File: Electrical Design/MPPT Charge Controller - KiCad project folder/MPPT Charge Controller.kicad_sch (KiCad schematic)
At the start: 70 parts, among them J1 Conn_01x02_Socket, J2 Conn_01x02_Socket, J3 Conn_01x02_Socket, Q1 Q_Dual_NMOS_S1G1S2G2D2D2D1D1, Q2 Q_Dual_NMOS_S1G1S2G2D2D2D1D1, Q3 2N7002, U2 AP63203WU, U3 ACS712, U4 ACS712, U5 MCP4018

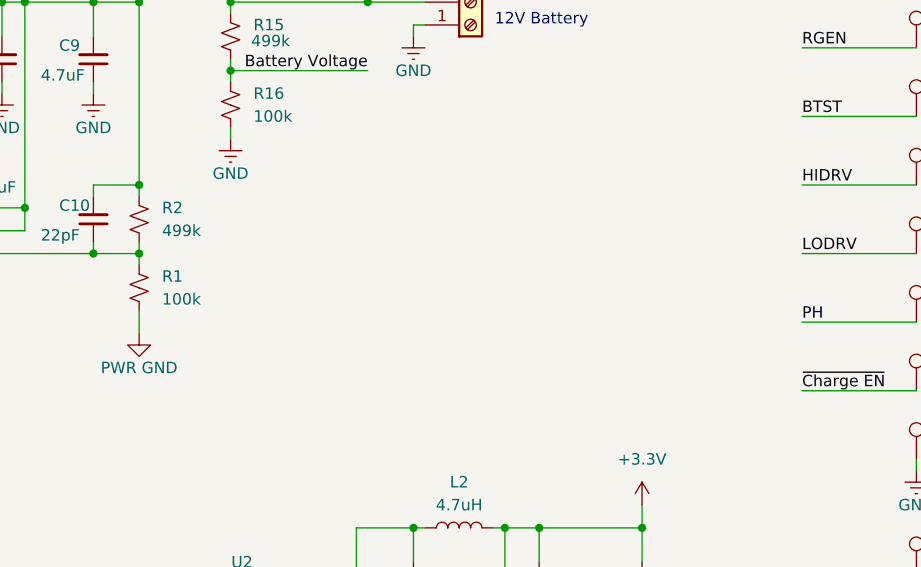
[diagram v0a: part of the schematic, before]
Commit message: update VBAT to 3.5V for single LiFePO4 cell
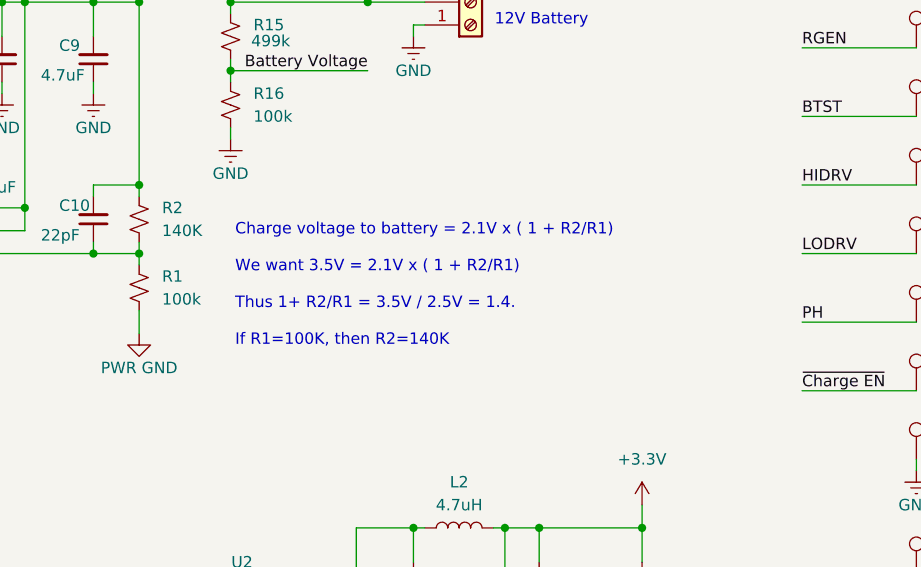
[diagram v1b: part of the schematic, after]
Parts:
- R2: value 499k -> 140K
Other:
- note added: "Charge voltage to battery = 2.1V x ( 1 + R2/R1) We want 3.5V = 2.1V x ( 1 + R2/R1) Thus 1+ R2/R1 = 3.5V / 2.5V = 1.4. If R1=100K, then R2=140K"
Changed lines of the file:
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@@
 	(title_block
 		(title "MPPT Charge Controller")
-		(rev "0.3")
+		(rev "20250209")
+		(comment 1 "Adapted for MEGAphone module format")
+		(comment 2 "Adapted for 3.5V output voltage")
 	)
 	(junction
@@
 		)
 	)
+	(text "Charge voltage to battery = 2.1V x ( 1 + R2/R1)\n\nWe want 3.5V = 2.1V x ( 1 + R2/R1)\n\nThus 1+ R2/R1 = 3.5V / 2.5V = 1.4.\n\nIf R1=100K, then R2=140K"
+		(exclude_from_sim no)
+		(at 194.818 102.616 0)
+		(effects
+			(font
+				(size 1.27 1.27)
+			)
+			(justify left)
+		)
+	)
 	(text "connected to GND\nthrough board vias"
 		(exclude_from_sim no)
@@
 	(label "STAT1"
 		(at 74.93 135.89 0)
-		(fields_autoplaced yes)
 		(effects
 			(font
@@
 	(label "BTST"
 		(at 257.81 83.82 0)
-		(fields_autoplaced yes)
 		(effects
 			(font
@@
 	(label "TS"
 		(at 257.81 43.18 0)
-		(fields_autoplaced yes)
 		(effects
 			(font
@@
 	(label "VCC"
 		(at 257.81 20.32 0)
-		(fields_autoplaced yes)
 		(effects
 			(font
@@
 	(label "SD_CS"
 		(at 74.93 143.51 0)
-		(fields_autoplaced yes)
 		(effects
 			(font
@@
 	(label "~{Charge EN}"
 		(at 74.93 140.97 0)
-		(fields_autoplaced yes)
 		(effects
 			(font
@@
 	(label "Input"
 		(at 34.29 45.72 0)
-		(fields_autoplaced yes)
 		(effects
 			(font
@@
 	(label "SCL"
 		(at 17.78 81.28 0)
-		(fields_autoplaced yes)
 		(effects
 			(font
@@
 	(label "Battery Voltage"
 		(at 209.55 78.74 180)
-		(fields_autoplaced yes)
 		(effects
 			(font
@@
 	(label "Solar Voltage"
 		(at 55.88 53.34 180)
-		(fields_autoplaced yes)
 		(effects
 			(font
@@
 	(label "Load Enable"
 		(at 240.03 55.88 180)
-		(fields_autoplaced yes)
 		(effects
 			(font
@@
 	(label "~{Charge EN}"
 		(at 52.07 78.74 0)
-		(fields_autoplaced yes)
 		(effects
 			(font
@@
 	(label "LODRV"
 		(at 257.81 99.06 0)
-		(fields_autoplaced yes)
 		(effects
 			(font
@@
 	(label "STAT2"
 		(at 257.81 67.31 0)
-		(fields_autoplaced yes)
 		(effects
 			(font
@@
 	(label "Load Enable"
 		(at 74.93 146.05 0)
-		(fields_autoplaced yes)
 		(effects
 			(font
@@
 	(label "HIDRV"
 		(at 257.81 91.44 0)
-		(fields_autoplaced yes)
 		(effects
 			(font
@@
 	(label "VCC"
 		(at 116.84 60.96 0)
-		(fields_autoplaced yes)
 		(effects
 			(font
@@
 	(label "Solar Voltage"
 		(at 134.62 151.13 180)
-		(fields_autoplaced yes)
 		(effects
 			(font
@@
 	(label "VREF"
 		(at 80.01 64.77 0)
-		(fields_autoplaced yes)
 		(effects
 			(font
@@
 	(label "MPPSET"
 		(at 71.12 72.39 0)
-		(fields_autoplaced yes)
 		(effects
 			(font
@@
 	(label "STAT2"
 		(at 83.82 99.06 180)
-		(fields_autoplaced yes)
 		(effects
 			(font
@@
 	(label "RGEN"
 		(at 257.81 76.2 0)
-		(fields_autoplaced yes)
 		(effects
 			(font
@@
 	(label "VFB"
 		(at 115.57 96.52 0)
-		(fields_autoplaced yes)
 		(effects
 			(font
@@
 	(label "Solar Current"
 		(at 31.75 19.05 0)
-		(fields_autoplaced yes)
 		(effects
 			(font
@@
 	(label "BTST"
 		(at 139.7 41.91 180)
-		(fields_autoplaced yes)
 		(effects
 			(font
@@
 	(label "VFB"
 		(at 257.81 50.8 0)
-		(fields_autoplaced yes)
 		(effects
 			(font
@@
 	(label "VIN"
 		(at 59.69 45.72 0)
-		(fields_autoplaced yes)
 		(effects
 			(font
@@
 	(label "TS"
 		(at 71.12 113.03 0)
-		(fields_autoplaced yes)
 		(effects
 			(font
@@
 	(label "HIDRV"
 		(at 116.84 53.34 0)
-		(fields_autoplaced yes)
 		(effects
 			(font
@@
 	(label "VIN"
 		(at 177.8 140.97 0)
-		(fields_autoplaced yes)
 		(effects
 			(font
@@
 	(label "Battery Voltage"
 		(at 134.62 156.21 180)
-		(fields_autoplaced yes)
 		(effects
 			(font
@@
 	(label "VREF"
 		(at 57.15 92.71 0)
-		(fields_autoplaced yes)
 		(effects
 			(font
@@
 	(label "Battery Current"
 		(at 134.62 158.75 180)
-		(fields_autoplaced yes)
 		(effects
 			(font
@@
 	(label "Input"
 		(at 257.81 135.89 0)
-		(fields_autoplaced yes)
 		(effects
 			(font
@@
 	(label "LODRV"
 		(at 116.84 81.28 0)
-		(fields_autoplaced yes)
 		(effects
 			(font
@@
 	(label "SDA"
 		(at 17.78 83.82 0)
-		(fields_autoplaced yes)
 		(effects
 			(font
@@
 	(label "STAT1"
 		(at 83.82 92.71 180)
-		(fields_autoplaced yes)
 		(effects
 			(font
@@
 	(label "~{Charge EN}"
 		(at 257.81 114.3 0)
-		(fields_autoplaced yes)
 		(effects
 			(font
@@
 	(label "RGEN"
 		(at 116.84 64.77 0)
-		(fields_autoplaced yes)
 		(effects
 			(font
@@
 	(label "STAT2"
 		(at 74.93 138.43 0)
-		(fields_autoplaced yes)
 		(effects
 			(font
@@
 	(label "PH"
 		(at 115.57 76.2 0)
-		(fields_autoplaced yes)
 		(effects
 			(font
@@
 	(label "VREF"
 		(at 257.81 27.94 0)
-		(fields_autoplaced yes)
 		(effects
 			(font
@@
 	(label "MPPSET"
 		(at 257.81 35.56 0)
-		(fields_autoplaced yes)
 		(effects
 			(font
@@
 	(label "PH"
 		(at 257.81 106.68 0)
-		(fields_autoplaced yes)
 		(effects
 			(font
@@
 	(label "SDA"
 		(at 74.93 176.53 0)
-		(fields_autoplaced yes)
 		(effects
 			(font
@@
 	(label "BTST"
 		(at 116.84 68.58 0)
-		(fields_autoplaced yes)
 		(effects
 			(font
@@
 	(label "RGEN"
 		(at 139.7 36.83 180)
-		(fields_autoplaced yes)
 		(effects
 			(font
@@
 	(label "SCL"
 		(at 74.93 179.07 0)
-		(fields_autoplaced yes)
 		(effects
 			(font
@@
 	(label "STAT1"
 		(at 257.81 58.42 0)
-		(fields_autoplaced yes)
 		(effects
 			(font
@@
 	(label "Solar Current"
 		(at 134.62 153.67 180)
-		(fields_autoplaced yes)
 		(effects
 			(font
@@
 	(label "Battery Current"
 		(at 175.26 44.45 0)
-		(fields_autoplaced yes)
 		(effects
 			(font
@@
 			)
 		)
-		(property "Value" "499k"
+		(property "Value" "140K"
 			(at 186.69 96.5199 0)
 			(effects

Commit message: continue to adapt for MEGAphone
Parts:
- removed J1, J2, J3: Conn_01x02_Socket, TerminalBlock:TerminalBlock_bornier-2_P5.08mm, symbol Connector:Screw_Terminal_01x02
- removed J4: ~, Connector_PinSocket_2.54mm:PinSocket_1x02_P2.54mm_Vertical, symbol Connector:Conn_01x02_Socket
- removed Q2: Q_Dual_NMOS_S1G1S2G2D2D2D1D1, Package_SO:PowerPAK_SO-8_Dual, symbol Device:Q_Dual_NMOS_S1G1S2G2D2D2D1D1
- removed TP1, TP10, TP11, TP12, TP13, TP2, TP3, TP4, TP5, TP6, TP7, TP8, TP9: TestPoint, TestPoint:TestPoint_Pad_D1.0mm, symbol Connector:TestPoint
- removed TP14, TP15: TestPoint, TestPoint:TestPoint_Loop_D2.60mm_Drill1.6mm_Beaded, symbol Connector:TestPoint
- added JP1, JP2: Jumper_2_Bridged, Jumper:SolderJumper-2_P1.3mm_Bridged_RoundedPad1.0x1.5mm, symbol Jumper:Jumper_2_Bridged
- added M2: ~, MegaCastle:MegaCastle2x23-Module-I30.0x53.6-M80000307FFFC, symbol MegaCastle:MegaCastle2x23-Module-I30.0x53.6-M80000307FFFC
- RSR1: value 0.02 -> 0.01
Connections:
- net +3.3V: now also JP1.2 (B), JP2.2 (B), M2.41; no longer R11.2, R14.2, U3.8 (VCC), U4.8 (VCC)
- net BTST: now also M2.33
- net GND: now also M2.23 (GND)
- net HIDRV: now also M2.32
- net Input: now also M2.24
- net LODRV: now also M2.31
- net MPPSET: now also M2.39
- net PH: now also M2.30
- net PWR GND: now also M2.44
- net RGEN: now also M2.34
- net STAT1: now also M2.43
- net STAT2: now also M2.42
- net TS: now also M2.38
- net VCC: now also M2.35
- net VFB: now also M2.37
- net VREF: now also M2.36
- net ~{Charge EN}: now also M2.40
- net VBAT_OUT: now reaches R15.1, U4.3 (IP-), U4.4 (IP-)
- net VBAT_OUT: now also M2.1 (VCC)
- net UART_RX: now reaches A1.14 (RX/IO16)
- net UART_RX: now also M2.46
- net UART_TX: now reaches A1.15 (TX/IO17)
- net UART_TX: now also M2.45
- net Load Enable: no longer names the net of A1.23 (D11)
- new net VCC_ACS712: JP1.1 (A), R14.2, U3.8 (VCC)
- new net VCC_ACS712_2: JP2.1 (A), R11.2, U4.8 (VCC)
- no-connect marks 19 -> 15
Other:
- note added: "3.6V LiFePO4 Cell"
- note added: "ACS712 Actually requires VCC = 5V, not 3.3V according to datasheet?"
- note added: "ACS712 Actually requires VCC = 5V, not 3.3V according to datasheet? People on the internet indicate that they seem to work fairly fine on VCC=3.3V, though."
- note added: "Develop 3.3V to power the ESP32 from the input side"
- note added: "OUTPUT FROM CHARGE SOURCE"
- note added: "RSR1 sets max charge current: I_MAX = 40mOhms / RSR1 20mOhms thus limits to 2A ACS712 on VCC=5V will have output on VIOUT to 3.3V ADC below 3.3V upto about 4A, or 7A if the 20A version of the ACS712 is used. Thus we can use 10mOhms to allow upto 4A charging. With a 10Ah LiFePO4 is his 0.4C, which is below the save limit of 1.0C"
- note removed: "12V Battery"
- note removed: "12V Load"
- note removed: "5V-28V Solar input"

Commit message: add silkscreen for all component values
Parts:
- Q1: value Q_Dual_NMOS_S1G1S2G2D2D2D1D1 -> SI7272DP
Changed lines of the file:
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@@
 			)
 		)
-		(property "Value" "Q_Dual_NMOS_S1G1S2G2D2D2D1D1"
+		(property "Value" "SI7272DP"
 			(at 153.67 54.6099 0)
 			(effects
@@
 			)
 		)
-		(property "Value" "Q_Dual_NMOS_S1G1S2G2D2D2D1D1"
+		(property "Value" "SI7272DP"
 			(at 153.67 82.5499 0)
 			(effects

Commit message: update module information on PCB
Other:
- title: MPPT Charge Controller -> MEGAphone MPPT Charge Controller
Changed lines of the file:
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@@
 	(paper "A4")
 	(title_block
-		(title "MPPT Charge Controller")
-		(rev "20250209")
+		(title "MEGAphone MPPT Charge Controller")
+		(rev "20250216")
 		(comment 1 "Adapted for MEGAphone module format")
 		(comment 2 "Adapted for 3.5V output voltage")

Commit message: switch to panelised footprint
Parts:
- M2: footprint MegaCastle:MegaCastle2x23-Module-I30.0x53.6-M80000307FFFC -> MegaCastle:MegaCastle2x23-Module-I30.0x53.6-M80000307FFFC-PANEL
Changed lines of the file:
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@@
 			)
 		)
-		(property "Footprint" "MegaCastle:MegaCastle2x23-Module-I30.0x53.6-M80000307FFFC"
+		(property "Footprint" "MegaCastle:MegaCastle2x23-Module-I30.0x53.6-M80000307FFFC-PANEL"
 			(at 242.57 92.71 0)
 			(effects
